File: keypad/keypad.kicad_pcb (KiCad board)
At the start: 2 copper layers, 60 x 63.2 mm, 60 parts, among them J1 NO FIT, P1 GT-USB-7010ASV, Q1 BC807-40LT1G, SW1 TS04-66-70-BK-100-SMT, SW2 TS04-66-70-BK-100-SMT, SW3 NO FIT, SW4 NO FIT, SW5 NO FIT, U1 RP2040, U3 W25Q16JVSSIQ, U4 NCP1117-3.3_SOT223, U5 DRV5053VAQDBZR, U6 DRV5053VAQDBZR, Y1 NX3225SA-12MHz-STD-CSR-6

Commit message: Make alterations for rev3
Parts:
- removed SW3: NO FIT, Jumper:SolderJumper-2_P1.3mm_Open_Pad1.0x1.5mm
- added C1: 100n, Capacitor_SMD:C_0805_2012Metric, B.Cu at (91.0, 101.0)
- added C2: 100n, Capacitor_SMD:C_0805_2012Metric, B.Cu at (118.8, 101.2)
- added C23: 47u, Capacitor_SMD:C_0805_2012Metric, F.Cu at (108.4, 68.0)
- added C24: 1n5, Capacitor_SMD:C_0805_2012Metric, F.Cu at (111.6, 73.2)
- added C25: 1n5, Capacitor_SMD:C_0805_2012Metric, F.Cu at (98.4, 73.2)
- added D10: SMLP14ECNWT86, LED_SMD:LED_0603_1608Metric, F.Cu at (96.4, 101.0)
- added J2: NO FIT, Connector_PinSocket_2.00mm:PinSocket_1x02_P2.00mm_Vertical, F.Cu at (84.4, 85.6)
- added R1: 1R, Resistor_SMD:R_0805_2012Metric, B.Cu at (98.8, 97.6)
- added R2: 200R, Resistor_SMD:R_0805_2012Metric, B.Cu at (95.8, 95.2)
- added TP1: NO FIT, TestPoint:TestPoint_Pad_1.5x1.5mm, F.Cu at (108.5, 100.8)
- added TP2: NO FIT, TestPoint:TestPoint_Pad_1.5x1.5mm, F.Cu at (105.0, 100.8)
- added U2: LM4040DBZ-2.0, Package_TO_SOT_SMD:SOT-23, B.Cu at (94.6, 98.6)
- C10, C5, C7: value 1u -> 2u2
- C17, C18: value 10u -> 47u
- J1: footprint Connector_PinHeader_1.27mm:PinHeader_1x02_P1.27mm_Vertical -> Connector_PinSocket_2.00mm:PinSocket_1x02_P2.00mm_Vertical
- R11, R12: value 27R -> 10K
- SW4, SW5: footprint Switch_Keyboard_Cherry_MX:SW_Cherry_MX_PCB_1.00u -> Button_Switch_Keyboard:SW_Cherry_MX_1.00u_PCB
- Y1: footprint Crystal:Crystal_SMD_3225-4Pin_3.2x2.5mm -> Custom_Footprints:Crystal_SMD_NX3225SA
- moved R11 28.9 mm to (114.6, 73.8), turned to -90 degrees
- moved R12 16.4 mm to (95.4, 73.8), turned to -90 degrees
- moved R13 13.2 mm to (94.4, 102.8), turned to -90 degrees
- moved C16 5.44 mm to (93.0, 91.2), turned to 180 degrees
- moved SW4 3.28 mm to (97.5, 77.3)
- moved SW5 3.28 mm to (117.5, 77.3)
- moved C18 1.41 mm to (96.8, 91.2), turned to 0 degrees
- moved C15 1.40 mm to (119.3, 75.6)
- moved J1 0.59 mm to (89.2, 110.0)
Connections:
- J1 pad 1: Net-(J1-Pad1) -> Net-(U1-Pad25)
- J1 pad 2: Net-(J1-Pad2) -> Net-(U1-Pad24)
- R11 pad 1: +3.3V -> Net-(U5-Pad2)
- R11 pad 2: ADC_AVDD -> ADC0
- R12 pad 1: ADC_AVDD -> Net-(U6-Pad2)
- R12 pad 2: Net-(R12-Pad2) -> ADC1
- R13 pad 1: Net-(R12-Pad2) -> Net-(D10-Pad1)
- U1 pad 24: Net-(J1-Pad1) -> Net-(U1-Pad24)
- U1 pad 25: Net-(J1-Pad2) -> Net-(U1-Pad25)
- U5 pad 2: ADC0 -> Net-(U5-Pad2)
- U6 pad 2: ADC1 -> Net-(U6-Pad2)
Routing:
- net Net-(U1-Pad25): track 0.00 -> 52.4 mm, vias 0 -> 2
- net Net-(J1-Pad1): track 27.3 -> 0.00 mm, vias 1 -> 0
- net Net-(J1-Pad2): track 24.6 -> 0.00 mm, vias 1 -> 0
- net ADC_AVDD: track 28.2 -> 10.2 mm, vias 2 -> 1
- net ADC1: track 44.6 -> 35.1 mm
- net ADC0: track 41.4 -> 35.7 mm, vias 0 -> 2
- net Net-(R1-Pad2): track 0.00 -> 5.31 mm
- net Net-(U5-Pad2): track 0.00 -> 4.39 mm
- net Net-(U6-Pad2): track 0.00 -> 4.31 mm
- net +3.3V: track 198.6 -> 202.5 mm
- net QSPI_SD3: track 22.0 -> 25.1 mm
- net VBUS: track 155.9 -> 158.4 mm
- net Net-(D10-Pad1): track 0.00 -> 2.08 mm
- net Net-(R12-Pad2): track 1.78 -> 0.00 mm
- net AUX1: track 32.9 -> 31.6 mm
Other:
- board text added: "pppad rev3"
- board text removed: "rev2 - prototype model"

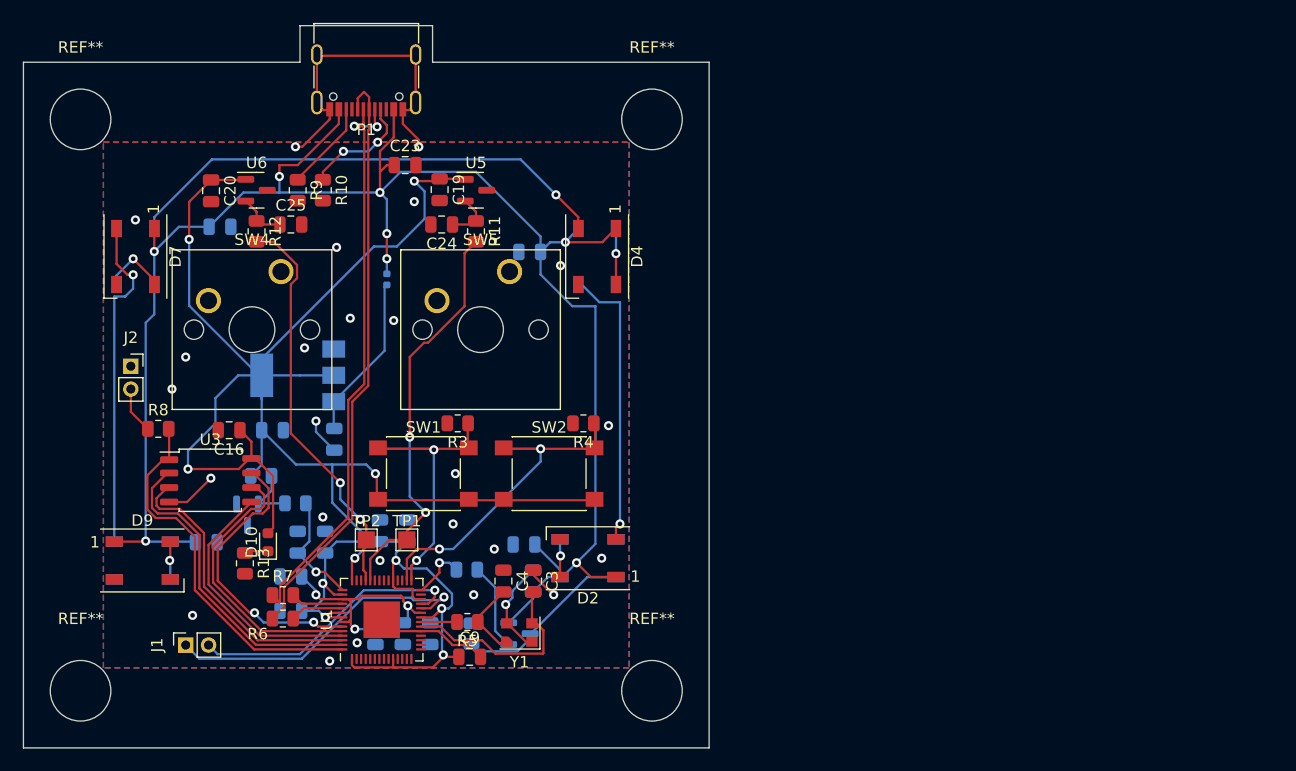
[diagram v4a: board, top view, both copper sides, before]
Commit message: ditch rev3a for rev3b
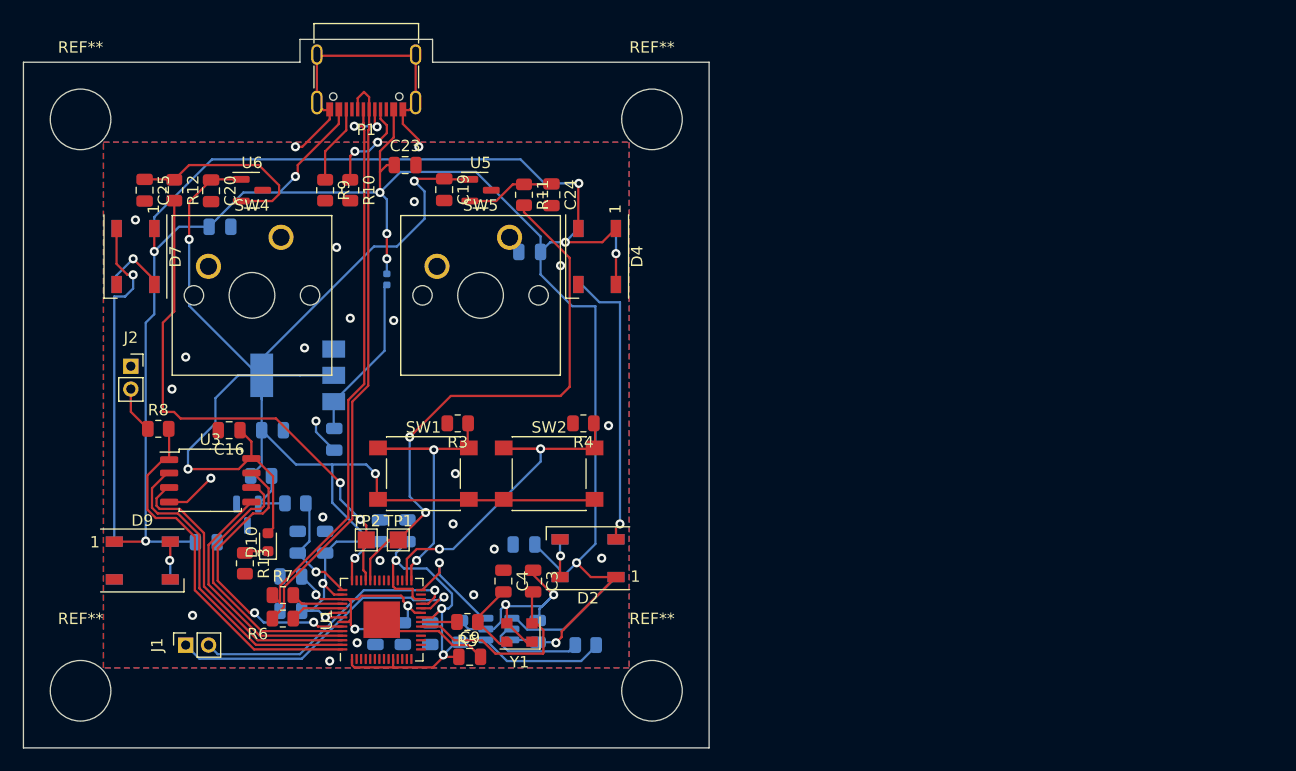
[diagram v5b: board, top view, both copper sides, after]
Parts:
- removed Q1: BC807-40LT1G, Package_TO_SOT_SMD:SOT-23
- removed R15: 10K, Resistor_SMD:R_0805_2012Metric
- added C26: 100n, Capacitor_SMD:C_0805_2012Metric, B.Cu at (113.2, 108.8)
- added U7: TXS0101DBVR, Package_TO_SOT_SMD:SOT-23-6, B.Cu at (116.6, 108.6)
- R14: value 1K -> 10K
- moved C25 13.1 mm to (85.6, 70.2), turned to -90 degrees
- moved R14 12.3 mm to (124.2, 110.0), turned to 180 degrees
- moved C24 9.95 mm to (121.2, 70.6), turned to -90 degrees
- moved R12 8.05 mm to (88.2, 70.2)
- moved R11 5.28 mm to (118.8, 70.6)
- moved C8 4.42 mm to (120.0, 108.8)
- moved SW4 3.00 mm to (97.5, 74.3)
- moved SW5 3.00 mm to (117.5, 74.3)
- moved R9 2.40 mm to (101.4, 70.2)
- moved R10 2.40 mm to (103.6, 70.2)
- moved TP1 0.75 mm to (107.8, 100.8)
- moved U5 0.40 mm to (115.0, 70.2)
- moved U6 0.40 mm to (95.0, 70.2)
- moved C19 0.40 mm to (111.8, 70.2)
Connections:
- R14 pad 1: RGB_D0 -> +3.3V
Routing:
- net Net-(J1-Pad1): track 52.4 -> 24.5 mm, vias 2 -> 1
- net Net-(J1-Pad2): track 0.00 -> 27.9 mm, vias 0 -> 1
- net +3.3V: track 202.5 -> 217.8 mm
- net ADC0: track 35.7 -> 49.0 mm
- net Net-(C25-Pad1): track 4.31 -> 17.4 mm
- net ADC1: track 35.1 -> 47.0 mm
- net GND: track 57.6 -> 67.0 mm
- net RGB_D0: track 4.85 -> 9.80 mm
- net VBUS: track 158.4 -> 162.9 mm, vias 8 -> 9
- net Net-(D1-Pad4): track 15.9 -> 11.4 mm
- net Net-(C24-Pad1): track 4.39 -> 7.76 mm
- net Net-(D4-Pad2): track 43.3 -> 45.1 mm
- net Net-(P1-PadA5): track 9.93 -> 8.35 mm
- net Net-(U7-Pad5): track 7.69 -> 8.90 mm
- net Net-(P1-PadB5): track 7.86 -> 6.86 mm
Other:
- board size 60 x 63.2 mm -> 60 x 62 mm
- board text added: "pppad rev3a"
- board text removed: "pppad rev3"

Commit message: initial placements for rev3b
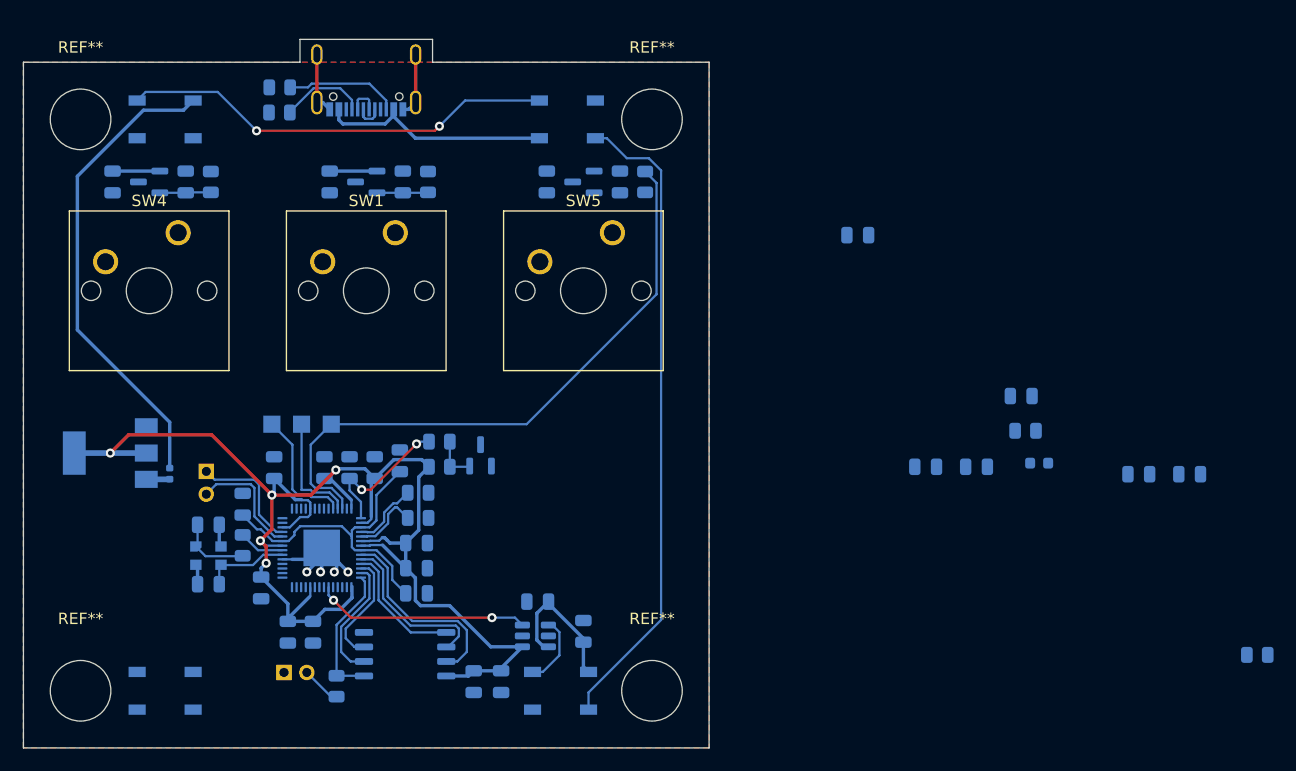
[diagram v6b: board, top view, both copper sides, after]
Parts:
- removed D5, D7, D8, D9: WS2812B-B/T, LED_SMD:LED_WS2812B_PLCC4_5.0x5.0mm_P3.2mm
- removed R4: 10K, Resistor_SMD:R_0805_2012Metric
- removed SW2: TS04-66-70-BK-100-SMT, Button_Switch_SMD:SW_Push_1P1T_NO_6x6mm_H9.5mm
- added C27: 100n, Capacitor_SMD:C_0805_2012Metric, B.Cu at (120.8, 69.5)
- added C28: 1n5, Capacitor_SMD:C_0805_2012Metric, B.Cu at (127.2, 69.5)
- added C29: 100n, Capacitor_SMD:C_0805_2012Metric, B.Cu at (100.3, 108.9)
- added C30: 100n, Capacitor_SMD:C_0805_2012Metric, B.Cu at (98.1, 108.9)
- added TP3: NO FIT, TestPoint:TestPoint_Pad_1.5x1.5mm, B.Cu at (101.9, 90.7)
- added U8: DRV5053VAQDBZR, Package_TO_SOT_SMD:SOT-23, B.Cu at (124.0, 69.5)
- C16, C19, C20, C23, C24, C25, C3, C4, C9, D10, D2, D4, J1, J2, P1, R10, R11, R12, R13, R3, R5, R6, R7, R8, R9, TP1, TP2, U1, U3, U5, U6, Y1: moved to B.Cu
- SW1: value TS04-66-70-BK-100-SMT -> NO FIT; footprint Button_Switch_SMD:SW_Push_1P1T_NO_6x6mm_H9.5mm -> Button_Switch_Keyboard:SW_Cherry_MX_1.00u_PCB
- moved C17 74.9 mm to (177.0, 95.0), turned to 180 degrees
- moved C23 69.7 mm to (172.6, 95.0), turned to 180 degrees
- moved R13 69.3 mm to (162.7, 91.2), turned to 180 degrees
- moved D10 67.8 mm to (163.9, 94.1), turned to 180 degrees
- moved C18 61.7 mm to (158.4, 94.4), turned to 180 degrees
- moved R14 58.8 mm to (183.0, 110.9)
- moved C13 55.8 mm to (148.0, 74.1), turned to 180 degrees
- moved D4 53.6 mm to (87.4, 114.0), turned to 180 degrees
- moved C2 45.4 mm to (162.3, 88.2)
- moved D3 39.7 mm to (87.4, 64.0), turned to 180 degrees
- moved C15 39.4 mm to (153.9, 94.4)
- moved D2 38.4 mm to (122.6, 64.0), turned to 0 degrees
- moved C1 33.9 mm to (124.0, 108.8), turned to 90 degrees
- moved C24 32.0 mm to (89.2, 69.5), turned to 90 degrees
- moved C16 30.7 mm to (114.4, 113.2), turned to -90 degrees
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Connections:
- D4 pad 2: Net-(D4-Pad2) -> unconnected-(D4-Pad2)
- R3 pad 1: AUX0 -> Net-(C28-Pad1)
- R3 pad 2: GND -> ADC2
- SW1 pad 1: AUX0 -> unconnected-(SW1-Pad1)
- SW1 pad 2: +3.3V -> unconnected-(SW1-Pad2)
- U1 pad 28: RGB_D0 -> unconnected-(U1-Pad28)
- U1 pad 29: AUX0 -> unconnected-(U1-Pad29)
- U1 pad 30: AUX1 -> unconnected-(U1-Pad30)
- U1 pad 40: unconnected-(U1-Pad40) -> ADC2
- U1 pad 6: unconnected-(U1-Pad6) -> RGB_D0
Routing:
- net VBUS: track 162.9 -> 75.3 mm, vias 9 -> 0
- net +3.3V: track 217.8 -> 134.1 mm, vias 10 -> 5
- net ADC2: track 0.00 -> 54.4 mm
- net Net-(D1-Pad2): track 3.34 -> 56.7 mm, vias 1 -> 0
- net USB_DN: track 51.6 -> 2.73 mm, vias 2 -> 0
- net USB_DP: track 51.6 -> 2.73 mm
- net Net-(D4-Pad2): track 45.1 -> 0.00 mm, vias 1 -> 0
- net ADC0: track 49.0 -> 11.0 mm, vias 2 -> 0
- net GND: track 67.0 -> 29.4 mm, vias 26 -> 4
- net ADC1: track 47.0 -> 10.00 mm, vias 2 -> 0
- net AUX1: track 31.6 -> 0.00 mm, vias 2 -> 0
- net Net-(D7-Pad2): track 29.5 -> 0.00 mm, vias 1 -> 0
- net AUX0: track 27.5 -> 0.00 mm, vias 2 -> 0
- net QSPI_SS: track 33.0 -> 12.2 mm
- net Net-(J1-Pad2): track 27.9 -> 10.4 mm, vias 1 -> 0
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- removed copper zone on B.Cu, net GND
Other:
- board text removed: "JLCJLCJLCJLC"
- board text removed: "pppad rev3a"

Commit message: finish rev3b
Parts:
- added R15: 10K, Resistor_SMD:R_0805_2012Metric, B.Cu at (120.4, 90.4)
- added R4: 10K, Resistor_SMD:R_0805_2012Metric, B.Cu at (107.4, 90.4)
- added SW2: TS04, Custom_Footprints:TS04, F.Cu at (111.0, 95.0)
- added SW3: TS04, Custom_Footprints:TS04, F.Cu at (124.0, 95.0)
- moved C17 91.9 mm to (85.2, 98.0)
- moved D10 81.6 mm to (82.6, 100.8), turned to 90 degrees
- moved C23 79.8 mm to (97.8, 67.2)
- moved C18 79.1 mm to (79.4, 98.8), turned to -90 degrees
- moved R13 78.0 mm to (85.4, 101.4), turned to 0 degrees
- moved C15 64.4 mm to (92.4, 113.4), turned to -90 degrees
- moved R14 59.4 mm to (123.8, 105.6)
- moved C13 56.3 mm to (92.4, 65.2), turned to -90 degrees
- moved C2 50.3 mm to (117.8, 64.8), turned to 90 degrees
- moved C16 3.67 mm to (111.2, 115.0), turned to 180 degrees
- moved C26 1.81 mm to (116.6, 111.4)
- renumbered REF** to Hole1, REF** to Hole2, REF** to Hole3, REF** to Hole4
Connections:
- U1 pad 7: unconnected-(U1-Pad7) -> AUX1
- U1 pad 8: unconnected-(U1-Pad8) -> AUX0
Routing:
- net GND: track 29.4 -> 137.3 mm, vias 4 -> 22
- net VBUS: track 75.3 -> 182.1 mm, vias 0 -> 6
- net +3.3V: track 134.1 -> 236.8 mm, vias 5 -> 11
- net Net-(D3-Pad2): track 0.00 -> 61.4 mm, vias 0 -> 2
- net USB_DP: track 2.73 -> 52.7 mm
- net USB_DN: track 2.73 -> 52.4 mm
- net AUX1: track 0.00 -> 34.1 mm, vias 0 -> 2
- net ADC1: track 10.00 -> 43.5 mm
- net AUX0: track 0.00 -> 32.8 mm, vias 0 -> 2
- net ADC0: track 11.0 -> 35.4 mm
- net Net-(R14-Pad2): track 0.00 -> 8.10 mm, vias 0 -> 2
- net Net-(C28-Pad1): track 0.00 -> 4.48 mm
- net Net-(C17-Pad1): track 2.06 -> 4.72 mm
- net Net-(D10-Pad1): track 0.00 -> 1.97 mm
- net Net-(D1-Pad4): track 6.20 -> 7.54 mm
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
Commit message: add helpful silkscreening
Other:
- board text added: "BOOTSEL"
- board text added: "JLCJLCJLCJLC"
- board text added: "SWCLK"
- board text added: "SWD"
- board text added: "pppad rev3b"
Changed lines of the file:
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@@
       (xy 110.8 57)
     ) (layer "Edge.Cuts") (width 0.1) (fill none))
+  (gr_text "SWCLK\n" (at 85.8 97.2) (layer "F.SilkS")
+    (effects (font (size 1.5 1.5) (thickness 0.3)))
+  )
+  (gr_text "BOOTSEL" (at 98.8 115.2) (layer "F.SilkS")
+    (effects (font (size 1.5 1.5) (thickness 0.3)))
+  )
+  (gr_text "SWD" (at 87.2 95) (layer "F.SilkS")
+    (effects (font (size 1.5 1.5) (thickness 0.3)))
+  )
+  (gr_text "pppad rev3b" (at 86.8 106.8) (layer "F.SilkS")
+    (effects (font (size 1.5 1.5) (thickness 0.3)))
+  )
+  (gr_text "JLCJLCJLCJLC\n" (at 86.8 104.4) (layer "F.SilkS")
+    (effects (font (size 1.5 1.5) (thickness 0.3)))
+  )
   (via (at 79.6 101.4) (size 0.8) (drill 0.4) (layers "F.Cu" "B.Cu") (net 1))
   (via (at 104.2 92.4) (size 0.8) (drill 0.4) (layers "F.Cu" "B.Cu") (net 1))
